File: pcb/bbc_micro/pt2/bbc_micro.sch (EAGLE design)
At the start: 51 parts, among them IC1 STM32F072C8T6, SW1 324_SW, SW2 324_SW, SW3 324_SW

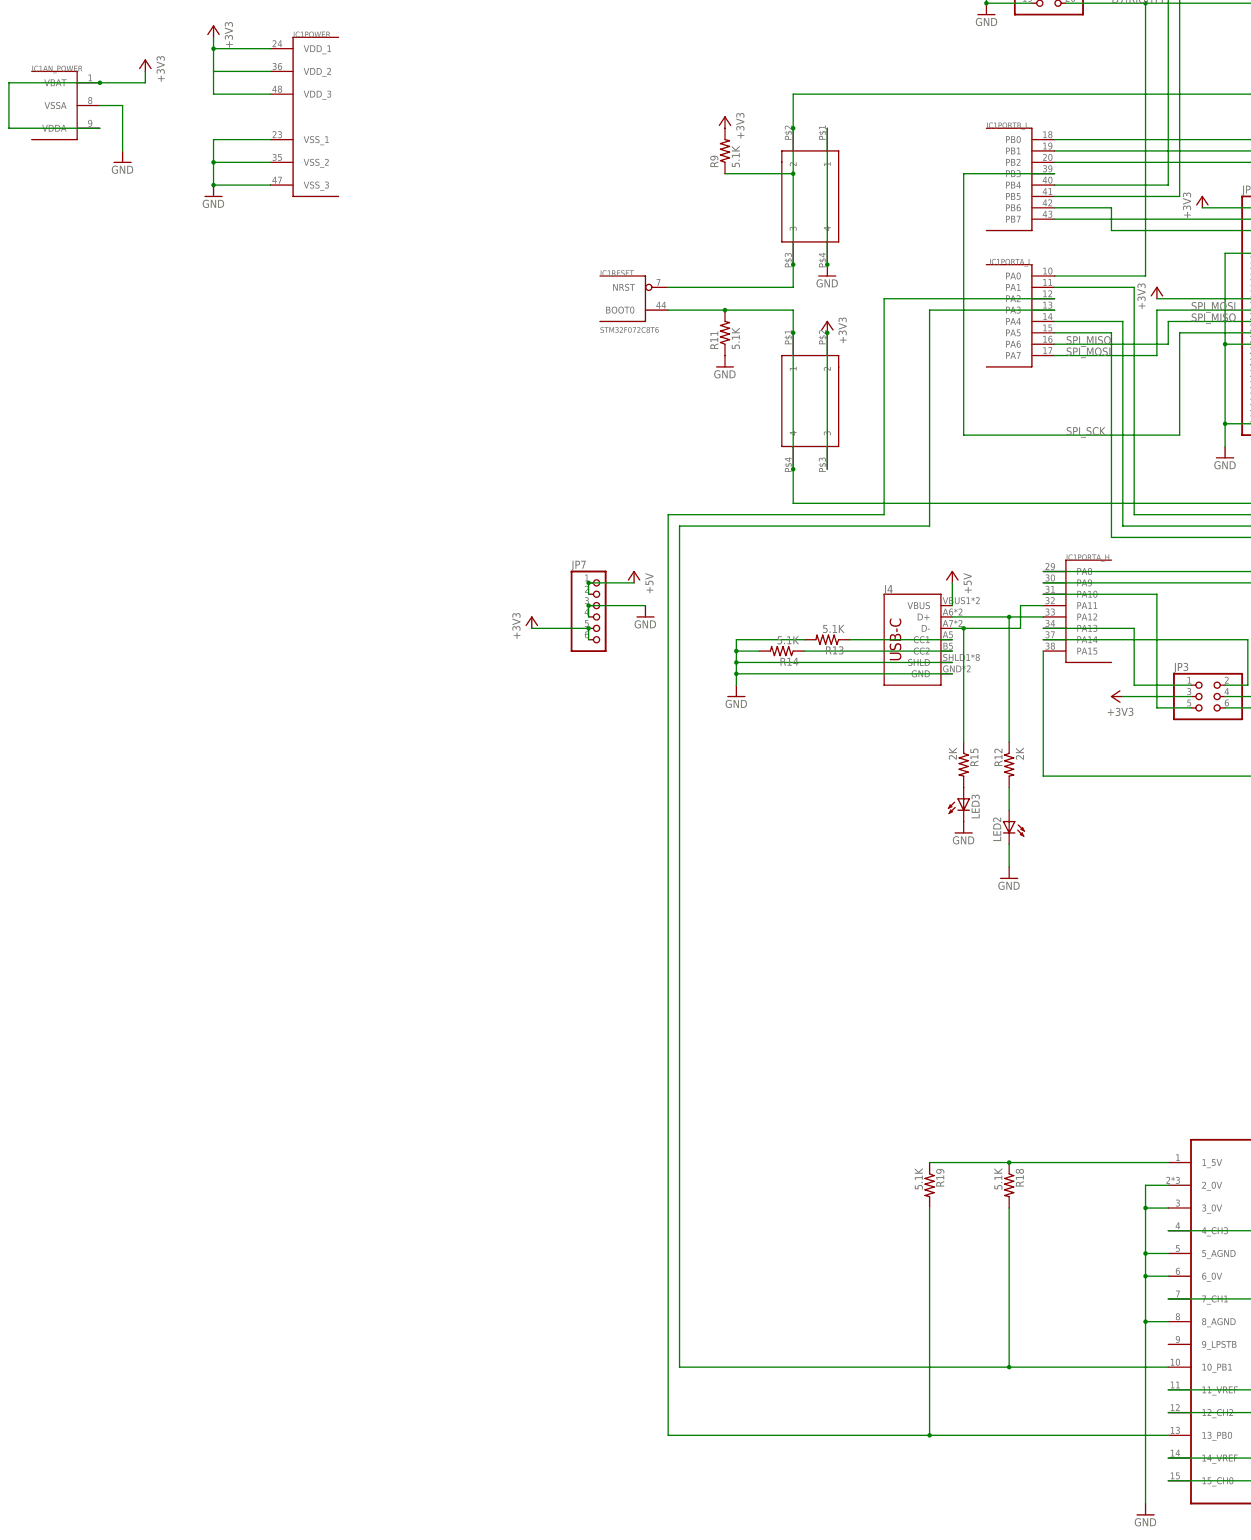
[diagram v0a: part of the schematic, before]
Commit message: fixed floating VDDA
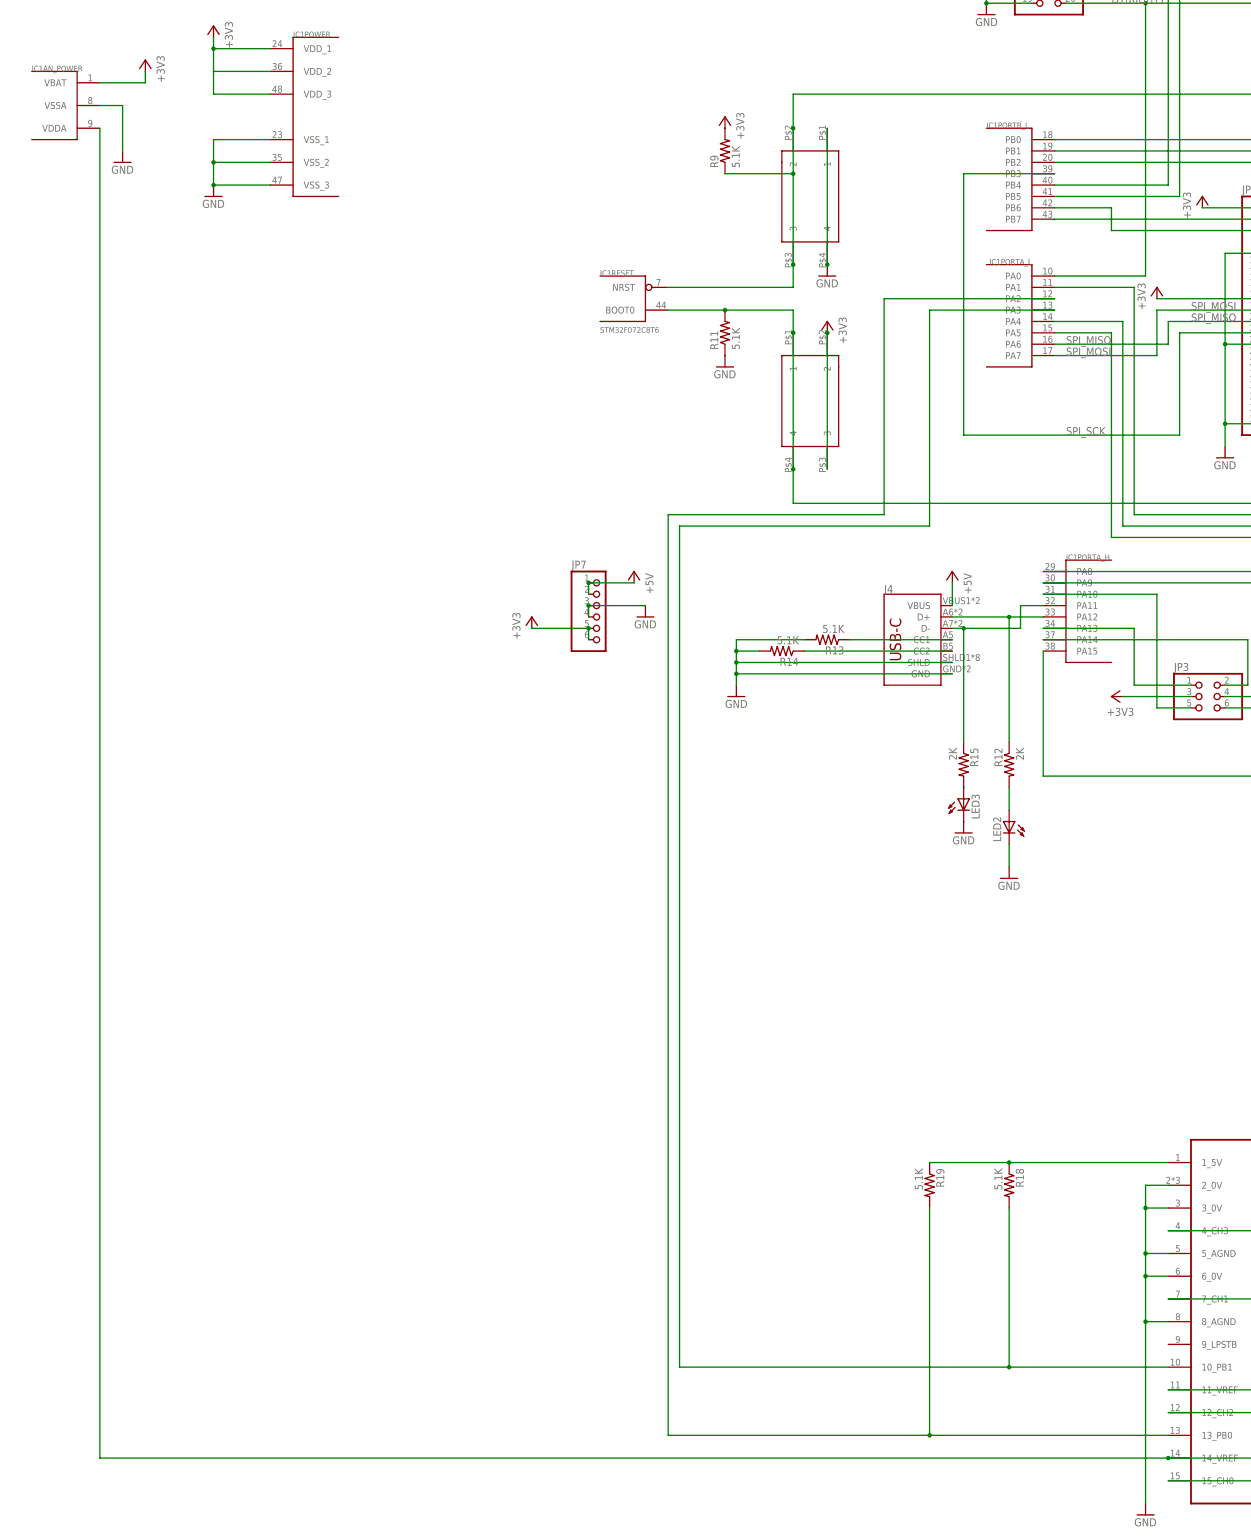
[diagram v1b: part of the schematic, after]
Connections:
- removed net N$10: R10.1, R17.1, U$9.11_VREF, U$9.14_VREF
- new net N$11: IC1AN_POWER.VDDA, R10.1, R17.1, U$9.11_VREF, U$9.14_VREF
- net +3V3: no longer IC1AN_POWER.VDDA
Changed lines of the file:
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@@
 <wire x1="-170.18" y1="71.12" x2="-160.02" y2="71.12" width="0.1524" layer="91"/>
 <wire x1="-160.02" y1="71.12" x2="-160.02" y2="73.66" width="0.1524" layer="91"/>
-<wire x1="-170.18" y1="71.12" x2="-190.5" y2="71.12" width="0.1524" layer="91"/>
-<wire x1="-190.5" y1="71.12" x2="-190.5" y2="60.96" width="0.1524" layer="91"/>
-<junction x="-170.18" y="71.12"/>
-<pinref part="IC1" gate="AN_POWER" pin="VDDA"/>
-<wire x1="-190.5" y1="60.96" x2="-170.18" y2="60.96" width="0.1524" layer="91"/>
 </segment>
 <segment>
@@
 </segment>
 </net>
+<net name="N$11" class="0">
+<segment>
+<pinref part="R17" gate="G$1" pin="1"/>
+<wire x1="187.96" y1="-185.42" x2="187.96" y2="-180.34" width="0.1524" layer="91"/>
+<pinref part="R10" gate="G$1" pin="1"/>
+<wire x1="187.96" y1="-180.34" x2="165.1" y2="-180.34" width="0.1524" layer="91"/>
+<wire x1="165.1" y1="-180.34" x2="165.1" y2="-185.42" width="0.1524" layer="91"/>
+<pinref part="U$9" gate="G$1" pin="14_VREF"/>
+<pinref part="IC1" gate="AN_POWER" pin="VDDA"/>
+<wire x1="-170.18" y1="60.96" x2="-170.18" y2="-236.22" width="0.1524" layer="91"/>
+<wire x1="-170.18" y1="-236.22" x2="68.58" y2="-236.22" width="0.1524" layer="91"/>
+<pinref part="U$9" gate="G$1" pin="11_VREF"/>
+<wire x1="68.58" y1="-220.98" x2="88.9" y2="-220.98" width="0.1524" layer="91"/>
+<wire x1="88.9" y1="-220.98" x2="88.9" y2="-236.22" width="0.1524" layer="91"/>
+<wire x1="88.9" y1="-236.22" x2="68.58" y2="-236.22" width="0.1524" layer="91"/>
+<junction x="68.58" y="-236.22"/>
+<wire x1="88.9" y1="-220.98" x2="119.38" y2="-220.98" width="0.1524" layer="91"/>
+<wire x1="119.38" y1="-220.98" x2="119.38" y2="-180.34" width="0.1524" layer="91"/>
+<junction x="88.9" y="-220.98"/>
+<wire x1="165.1" y1="-180.34" x2="119.38" y2="-180.34" width="0.1524" layer="91"/>
+<junction x="165.1" y="-180.34"/>
+</segment>
+</net>
 <net name="N$17" class="0">
 <segment>
@@
 </segment>
 </net>
-<net name="N$10" class="0">
-<segment>
-<pinref part="U$9" gate="G$1" pin="14_VREF"/>
-<wire x1="88.9" y1="-236.22" x2="68.58" y2="-236.22" width="0.1524" layer="91"/>
-<pinref part="U$9" gate="G$1" pin="11_VREF"/>
-<wire x1="68.58" y1="-220.98" x2="88.9" y2="-220.98" width="0.1524" layer="91"/>
-<wire x1="88.9" y1="-220.98" x2="88.9" y2="-236.22" width="0.1524" layer="91"/>
-<junction x="88.9" y="-220.98"/>
-<wire x1="88.9" y1="-220.98" x2="119.38" y2="-220.98" width="0.1524" layer="91"/>
-<wire x1="119.38" y1="-220.98" x2="119.38" y2="-180.34" width="0.1524" layer="91"/>
-<pinref part="R10" gate="G$1" pin="1"/>
-<wire x1="165.1" y1="-180.34" x2="165.1" y2="-185.42" width="0.1524" layer="91"/>
-<wire x1="165.1" y1="-180.34" x2="119.38" y2="-180.34" width="0.1524" layer="91"/>
-<junction x="165.1" y="-180.34"/>
-<wire x1="187.96" y1="-180.34" x2="165.1" y2="-180.34" width="0.1524" layer="91"/>
-<pinref part="R17" gate="G$1" pin="1"/>
-<wire x1="187.96" y1="-185.42" x2="187.96" y2="-180.34" width="0.1524" layer="91"/>
-</segment>
-</net>
